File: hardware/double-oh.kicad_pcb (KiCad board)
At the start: 2 copper layers, 81.6 x 14 mm, 42 parts, among them J1 USB_B_Micro, J10 Conn_01x01, J11 Conn_01x01, J2 Conn_01x01, J3 Conn_01x01, J4 Conn_01x01, J5 Conn_01x01, J6 Conn_01x01, J7 Conn_01x01, J8 Conn_01x01, J9 Conn_01x01, Q1 Q_PMOS_GSD, Q2 Q_DUAL_NPN_NPN_E1B1C2E2B2C1, U1 AP2127N-3.3, U2 MCP4017-xxxx, U3 MCP73831-2-OT, U4 LMV321, U5 ESP8285, U6 CP2105, Y1 26MHz

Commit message: Update i2c net names
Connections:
- net digipot_sclk renamed i2c_sda
- net digipot_u~d renamed i2c_scl

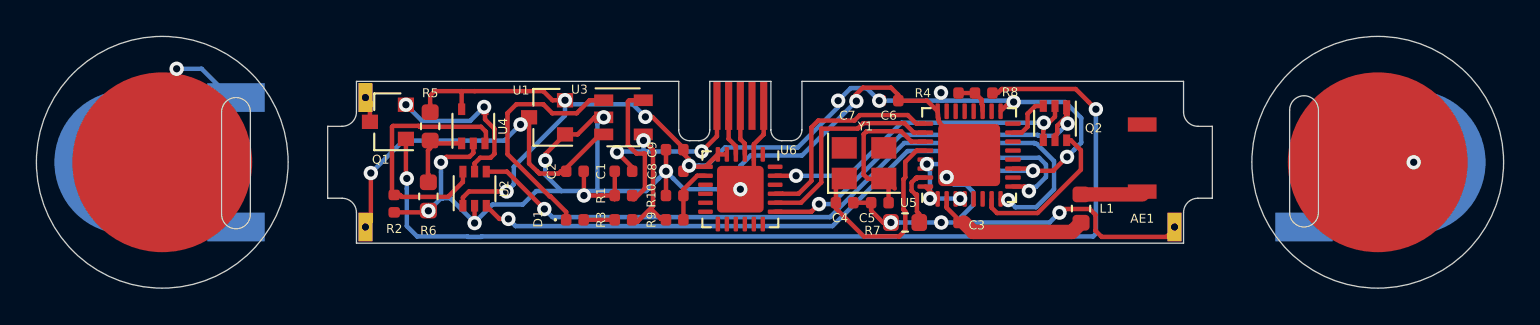
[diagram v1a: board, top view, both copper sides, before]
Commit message: Added a factory-reset pad to hardware
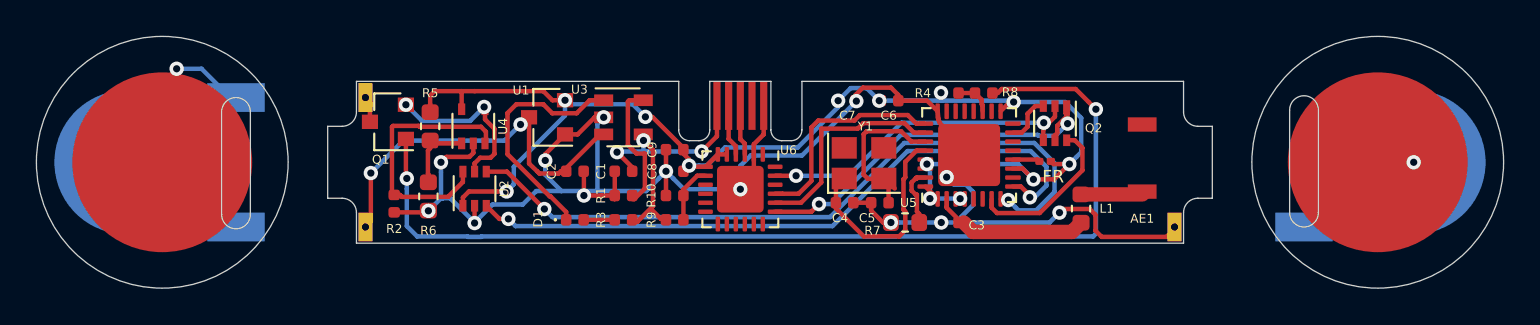
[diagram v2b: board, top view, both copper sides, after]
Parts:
- added FR: 1GΩ, Resistor_SMD:R_0201_0603Metric, F.Cu at (138.3, 104.5)
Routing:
- net 3.3V: track 74.4 -> 76.4 mm
- net Net-(R11-Pad1): track 0.00 -> 1.51 mm
- net i2c_scl: track 36.7 -> 37.3 mm

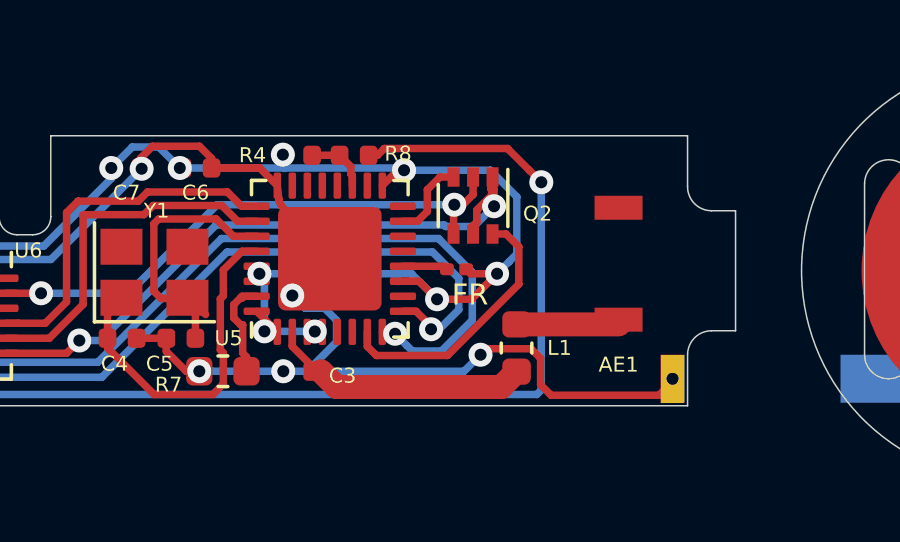
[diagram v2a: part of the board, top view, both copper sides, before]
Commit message: Updated factory reset hardware to work with factory reset firmware
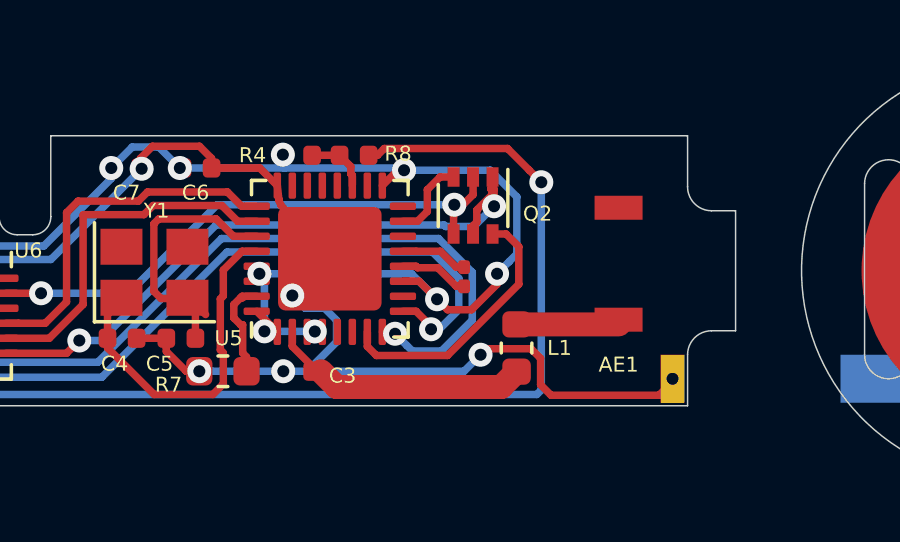
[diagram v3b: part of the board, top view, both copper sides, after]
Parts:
- moved R11 0.35 mm to (138.6, 104.7), turned to 90 degrees
- renumbered FR to R11
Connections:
- R11 pad 2: 3.3V -> Net-(R11-Pad2)
- U5 pad 13: Net-(U5-Pad13) -> Net-(R11-Pad2)
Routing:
- net Net-(R11-Pad2): track 0.00 -> 2.26 mm
- net Net-(R11-Pad1): track 1.51 -> 2.32 mm
- net 3.3V: track 76.4 -> 75.8 mm

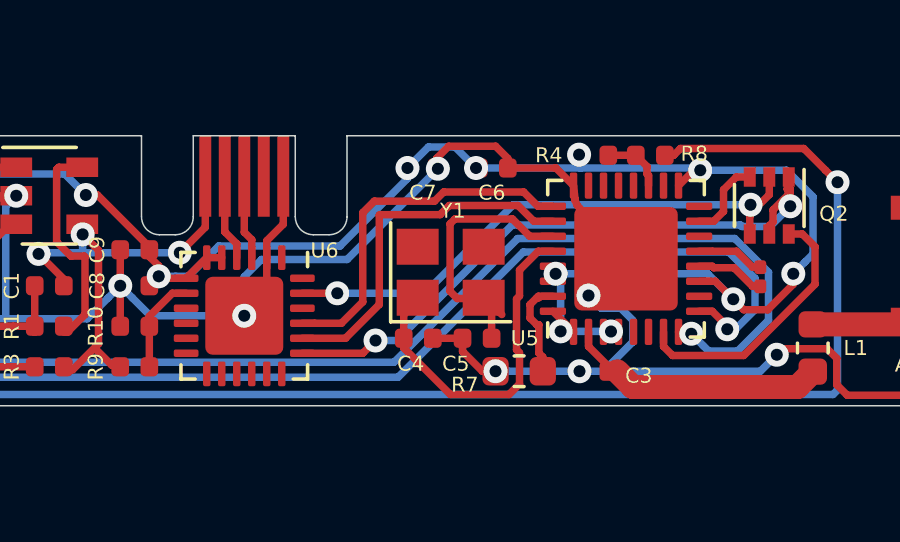
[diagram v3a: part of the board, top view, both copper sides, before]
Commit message: Fixed crystal layout and routing
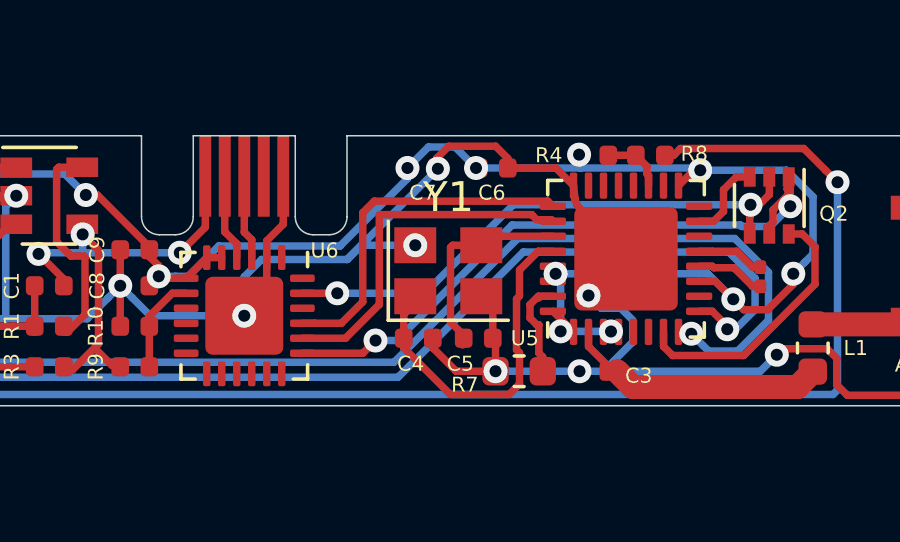
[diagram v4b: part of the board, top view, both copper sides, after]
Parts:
- Y1: value 26MHz -> Crystal_GND24; footprint Crystal:Crystal_SMD_TXC_7M-4Pin_3.2x2.5mm -> Crystal:Crystal_SMD_3225-4Pin_3.2x2.5mm
- moved Y1 0.09 mm to (128.2, 104.5)
- turned C5 to 0 degrees
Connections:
- Y1 pad 2: Net-(C5-Pad1) -> 0V
- Y1 pad 3: (no net) -> Net-(C5-Pad1)
- Y1 pad 4: (no net) -> 0V
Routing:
- net 0V: track 95.7 -> 100.6 mm, vias 13 -> 14
- net Net-(C5-Pad1): track 9.49 -> 7.00 mm

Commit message: Update main board gerbers
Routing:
- net to_top_cap: track 2.02 -> 1.45 mm
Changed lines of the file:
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@@
     (thickness 0.6)
     (drawings 58)
-    (tracks 506)
+    (tracks 505)
     (zones 0)
     (modules 43)
@@
   (segment (start 116.362659 103.687339) (end 115.96266 103.28734) (width 0.25) (layer F.Cu) (net 2))
   (segment (start 115.335 105) (end 115.335 104.780819) (width 0.25) (layer F.Cu) (net 2))
+  (segment (start 128.625 106.75) (end 128.625 106.975) (width 0.25) (layer F.Cu) (net 3))
+  (segment (start 128.3 103.65) (end 129.25 103.65) (width 0.25) (layer F.Cu) (net 3))
+  (segment (start 128.224999 103.725001) (end 128.3 103.65) (width 0.25) (layer F.Cu) (net 3))
+  (segment (start 128.224999 106.210001) (end 128.224999 103.725001) (width 0.25) (layer F.Cu) (net 3))
+  (segment (start 128.665 106.650002) (end 128.224999 106.210001) (width 0.25) (layer F.Cu) (net 3))
+  (segment (start 128.665 106.75) (end 128.665 106.650002) (width 0.25) (layer F.Cu) (net 3))
+  (segment (start 129.55 103.35) (end 129.25 103.65) (width 0.25) (layer F.Cu) (net 3))
+  (segment (start 131.6375 103.35) (end 129.55 103.35) (width 0.25) (layer F.Cu) (net 3))
   (segment (start 114.365 107.7) (end 112.635 107.7) (width 0.25) (layer F.Cu) (net 4))
   (segment (start 112.97 101.05) (end 113.75 101.05) (width 0.25) (layer F.Cu) (net 5))
@@
   (segment (start 111.37 105) (end 111.665 105) (width 0.25) (layer F.Cu) (net 7))
   (via (at 132.525 107.85) (size 0.8) (drill 0.4) (layers F.Cu B.Cu) (net 8))
-  (via (at 106.57 107.88) (size 0.8) (drill 0.4) (layers F.Cu B.Cu) (net 8))
   (via (at 104.7 104.5) (size 0.8) (drill 0.4) (layers F.Cu B.Cu) (net 8))
   (via (at 110.5 104.4) (size 0.8) (drill 0.4) (layers F.Cu B.Cu) (net 8))
@@
   (segment (start 140.781484 107.09999) (end 141.10001 107.418516) (width 0.25) (layer F.Cu) (net 8))
   (segment (start 106.5 103.6) (end 106.5 103.98359) (width 0.25) (layer F.Cu) (net 8))
-  (segment (start 106.57 107.85) (end 106.57 107.88) (width 0.25) (layer B.Cu) (net 8))
   (segment (start 110 106.1) (end 109.25 106.85) (width 0.25) (layer B.Cu) (net 8))
   (segment (start 138.55 107.85) (end 139.1 107.3) (width 0.25) (layer B.Cu) (net 8))
@@
   (segment (start 110.5 104.4) (end 110.5 104.05) (width 0.25) (layer F.Cu) (net 8))
   (segment (start 106.5 103.98359) (end 106.28359 104.2) (width 0.25) (layer F.Cu) (net 8))
-  (segment (start 106.57 107.88) (end 106.57 106.92) (width 0.25) (layer F.Cu) (net 8))
   (segment (start 104.8 106.5) (end 104.7 106.4) (width 0.25) (layer B.Cu) (net 8))
   (segment (start 110.5 104.4) (end 110.5 105.2) (width 0.25) (layer B.Cu) (net 8))
@@
   (segment (start 117.215972 104.025972) (end 117.215 104.025) (width 0.25) (layer F.Cu) (net 8))
   (segment (start 124.777644 104.12501) (end 121.92499 104.12501) (width 0.25) (layer B.Cu) (net 8))
-  (segment (start 128.625 106.75) (end 128.625 106.975) (width 0.25) (layer F.Cu) (net 3))
-  (segment (start 128.3 103.65) (end 129.25 103.65) (width 0.25) (layer F.Cu) (net 3))
-  (segment (start 128.224999 103.725001) (end 128.3 103.65) (width 0.25) (layer F.Cu) (net 3))
-  (segment (start 128.224999 106.210001) (end 128.224999 103.725001) (width 0.25) (layer F.Cu) (net 3))
-  (segment (start 128.665 106.650002) (end 128.224999 106.210001) (width 0.25) (layer F.Cu) (net 3))
-  (segment (start 128.665 106.75) (end 128.665 106.650002) (width 0.25) (layer F.Cu) (net 3))
-  (segment (start 129.55 103.35) (end 129.25 103.65) (width 0.25) (layer F.Cu) (net 3))
-  (segment (start 131.6375 103.35) (end 129.55 103.35) (width 0.25) (layer F.Cu) (net 3))
   (segment (start 134.299001 106.874001) (end 134.300001 106.873001) (width 0.25) (layer B.Cu) (net 8))
   (segment (start 122.1 105.25) (end 121.35 106) (width 0.25) (layer F.Cu) (net 8))
@@
   (segment (start 125.252654 103.65) (end 127.05 103.65) (width 0.25) (layer B.Cu) (net 8))
   (segment (start 124.777644 104.12501) (end 125.252654 103.65) (width 0.25) (layer B.Cu) (net 8))
+  (segment (start 106.57 107.85) (end 106.57 107.88) (width 0.25) (layer B.Cu) (net 8))
+  (via (at 106.57 107.88) (size 0.8) (drill 0.4) (layers F.Cu B.Cu) (net 8))
+  (segment (start 106.57 107.88) (end 106.57 106.92) (width 0.25) (layer F.Cu) (net 8))
   (segment (start 128.22 108.625) (end 130.175 108.625) (width 0.25) (layer F.Cu) (net 9))
   (segment (start 130.42498 107.13639) (end 130.52499 107.2364) (width 0.25) (layer F.Cu) (net 9))
@@
   (via (at 102.8 105.4) (size 0.8) (drill 0.4) (layers F.Cu B.Cu) (net 14))
   (via (at 141.125 101.55) (size 0.8) (drill 0.4) (layers F.Cu B.Cu) (net 14))
-  (segment (start 103.375 108.625) (end 102.8 108.05) (width 0.25) (layer B.Cu) (net 14))
-  (segment (start 140.975 108.625) (end 106.968004 108.625) (width 0.25) (layer B.Cu) (net 14))
-  (segment (start 141.125 108.475) (end 140.975 108.625) (width 0.25) (layer B.Cu) (net 14))
-  (segment (start 106.943014 108.64999) (end 106.196986 108.64999) (width 0.25) (layer B.Cu) (net 14))
-  (segment (start 106.196986 108.64999) (end 106.171996 108.625) (width 0.25) (layer B.Cu) (net 14))
-  (segment (start 102.8 108.05) (end 102.8 105.965685) (width 0.25) (layer B.Cu) (net 14))
-  (segment (start 102.8 105.965685) (end 102.8 105.4) (width 0.25) (layer B.Cu) (net 14))
-  (segment (start 141.125 101.55) (end 141.125 108.475) (width 0.25) (layer B.Cu) (net 14))
-  (segment (start 106.171996 108.625) (end 103.375 108.625) (width 0.25) (layer B.Cu) (net 14))
   (segment (start 135.37 100.65) (end 135.665 100.65) (width 0.25) (layer F.Cu) (net 14))
   (segment (start 139.999999 100.424999) (end 140.725001 101.150001) (width 0.25) (layer F.Cu) (net 14))
   (segment (start 135.665 100.65) (end 135.890001 100.424999) (width 0.25) (layer F.Cu) (net 14))
   (segment (start 102.75 103.2) (end 102.75 105.35) (width 0.25) (layer F.Cu) (net 14))
-  (segment (start 106.968004 108.625) (end 106.943014 108.64999) (width 0.25) (layer B.Cu) (net 14))
   (segment (start 140.725001 101.150001) (end 141.125 101.55) (width 0.25) (layer F.Cu) (net 14))
   (segment (start 135.890001 100.424999) (end 139.999999 100.424999) (width 0.25) (layer F.Cu) (net 14))
   (segment (start 102.75 105.35) (end 102.8 105.4) (width 0.25) (layer F.Cu) (net 14))
+  (segment (start 106.943014 108.64999) (end 106.196986 108.64999) (width 0.25) (layer B.Cu) (net 14))
+  (segment (start 106.968004 108.625) (end 106.943014 108.64999) (width 0.25) (layer B.Cu) (net 14))
+  (segment (start 141.125 101.55) (end 141.125 108.475) (width 0.25) (layer B.Cu) (net 14))
+  (segment (start 106.196986 108.64999) (end 106.171996 108.625) (width 0.25) (layer B.Cu) (net 14))
+  (segment (start 140.975 108.625) (end 106.968004 108.625) (width 0.25) (layer B.Cu) (net 14))
+  (segment (start 102.8 105.965685) (end 102.8 105.4) (width 0.25) (layer B.Cu) (net 14))
+  (segment (start 141.125 108.475) (end 140.975 108.625) (width 0.25) (layer B.Cu) (net 14))
+  (segment (start 106.171996 108.625) (end 103.375 108.625) (width 0.25) (layer B.Cu) (net 14))
+  (segment (start 103.375 108.625) (end 102.8 108.05) (width 0.25) (layer B.Cu) (net 14))
+  (segment (start 102.8 108.05) (end 102.8 105.965685) (width 0.25) (layer B.Cu) (net 14))
   (via (at 107.1 101.425) (size 0.8) (drill 0.4) (layers F.Cu B.Cu) (net 15))
   (segment (start 107.15 102.11359) (end 107.675001 102.638591) (width 0.25) (layer F.Cu) (net 15))
@@
   (segment (start 158.8 104.5) (end 154.800001 108.499999) (width 0.25) (layer B.Cu) (net 53))
   (segment (start 153.099999 108.499999) (end 153.014102 108.414101) (width 0.25) (layer B.Cu) (net 53))
-  (segment (start 100.9 101.3) (end 100.5 100.9) (width 0.25) (layer F.Cu) (net 54))
   (segment (start 100.75 101.15) (end 100.5 100.9) (width 0.25) (layer F.Cu) (net 54))
   (segment (start 100.75 102.25) (end 100.75 101.15) (width 0.25) (layer F.Cu) (net 54))

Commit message: Update crystal caps
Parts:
- C4, C5: value 5.6pF -> 10pF
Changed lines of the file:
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@@
       (effects (font (size 0.5 0.5) (thickness 0.1)))
     )
-    (fp_text value 5.6pF (at 0 1.17) (layer F.Fab)
+    (fp_text value 10pF (at 0 1.17) (layer F.Fab)
       (effects (font (size 1 1) (thickness 0.15)))
     )
@@
       (effects (font (size 0.5 0.5) (thickness 0.1)))
     )
-    (fp_text value 5.6pF (at 0 1.17) (layer F.Fab)
+    (fp_text value 10pF (at 0 1.17) (layer F.Fab)
       (effects (font (size 1 1) (thickness 0.15)))
     )

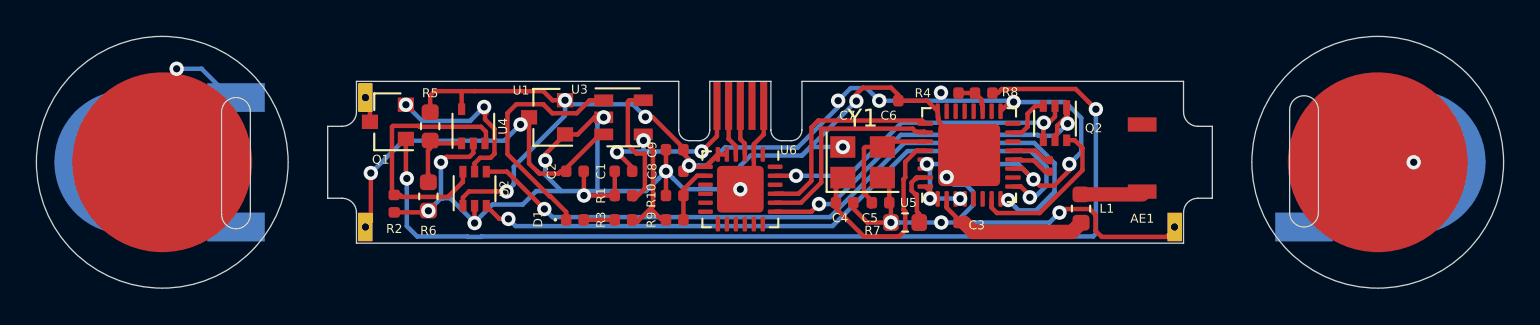
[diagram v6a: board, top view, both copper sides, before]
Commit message: Increased text size for legibility
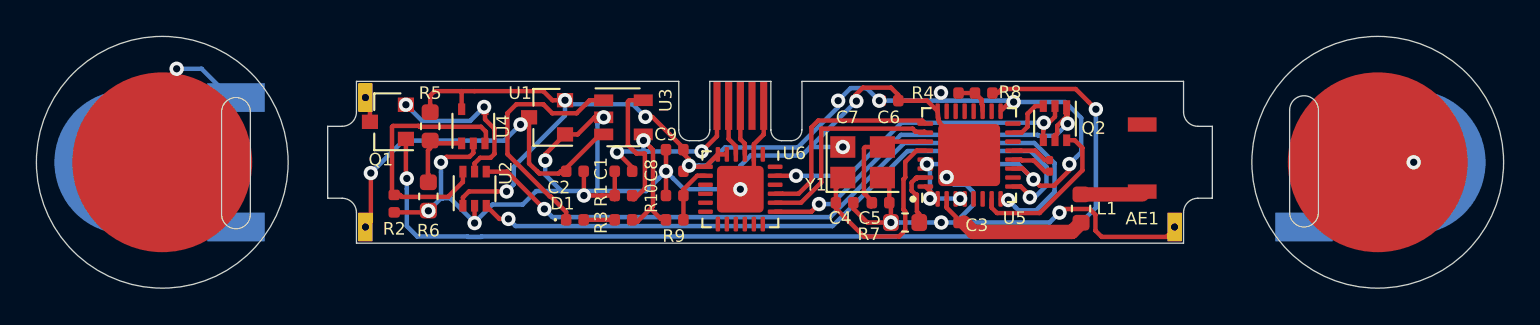
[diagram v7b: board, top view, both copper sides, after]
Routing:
- net Net-(Q1-Pad1): track 56.8 -> 55.9 mm

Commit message: Working on a version that, y'know, would actually work
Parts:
- removed the R2 at (102.1, 106.8)
- removed the R5 at (104.1, 102.5)
- removed the R6 at (104.0, 106.4)
- removed the U3 at (114.8, 102.0)
- removed the U4 at (106.5, 102.5)
- added ?: Conn_01x01, powerplay:cap_board_solder_mount, B.Cu at (152.7, 100.9)
- added ?: Conn_01x01, powerplay:main_board_solder_mount, F.Cu at (145.5, 100.9)
- added C10: 10μF, Capacitor_SMD:C_0402_1005Metric, F.Cu at (108.7, 104.0)
- added C11: 4.7μF, Capacitor_SMD:C_0402_1005Metric, F.Cu at (106.7, 107.8)
- added C12: 4.7μF, Capacitor_SMD:C_0402_1005Metric, F.Cu at (105.8, 102.4)
- added C13: 10μF, Capacitor_SMD:C_0402_1005Metric, F.Cu at (104.1, 106.0)
- added L2: 2.2 μH, Inductor_SMD:L_0402_1005Metric, F.Cu at (108.7, 106.1)
- added L3: 2.2 μH, Inductor_SMD:L_0402_1005Metric, F.Cu at (104.1, 104.0)
- added R10: 67 kΩ, Resistor_SMD:R_0402_1005Metric, F.Cu at (107.0, 100.7)
- added R11: 100 kΩ, Resistor_SMD:R_0402_1005Metric, F.Cu at (103.0, 106.0)
- added R9: 300 kΩ, Resistor_SMD:R_0402_1005Metric, F.Cu at (108.8, 101.8)
- added U5: MP2109, Package_DFN_QFN:DFN-10-1EP_3x3mm_P0.5mm_EP1.7x2.5mm, F.Cu at (106.3, 105.0)
- U1: value AP2127N-3.3 -> MCP73831-2-OT; footprint Package_TO_SOT_SMD:SOT-23 -> Package_TO_SOT_SMD:SOT-23-5
- moved U3 4.73 mm to (111.3, 105.8), turned to 0 degrees
- moved U1 4.25 mm to (114.8, 102.0), turned to 0 degrees
- moved C2 2.57 mm to (112.5, 102.5), turned to 270 degrees
- moved D1 1.27 mm to (113.4, 107.7)
- moved R4 0.67 mm to (115.5, 107.7)
- renumbered C8 to C3, C9 to C4, C6 to C5, C7 to C6, C3 to C7, C4 to C8, C5 to C9, Q2 to Q1, Q1 to Q2, R9 to R1, R1 to R2, R10 to R3, R3 to R4, R7 to R5, R11 to R6, R4 to R7, U6 to U2, U2 to U3, U5 to U4
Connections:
- R2 pad 2: Net-(R1-Pad2) (its old number) -> Net-(R2-Pad2)
- U1 pad 1: 0V -> Net-(D1-Pad1)
- U1 pad 2: 3.3V -> 0V
- U2 pad 5: Net-(U6-Pad5) -> 3.3V
- U3 pad 5: batt_out -> digipot2
- U3 pad 6: digipot1 -> 0V
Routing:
- net digipot1: track 14.8 -> 0.00 mm
- net digipot2: track 0.00 -> 14.7 mm, vias 0 -> 3
- net 3.3V: track 75.8 -> 65.5 mm, vias 13 -> 12
- net LIPO_V: track 21.2 -> 30.4 mm, vias 2 -> 3
- net Net-(R1-Pad2) (its old number): track 7.32 -> 0.00 mm
- net Net-(R2-Pad2): track 0.00 -> 7.01 mm
- net 0V: track 100.6 -> 94.6 mm, vias 14 -> 12
- net i2c_sda: track 40.1 -> 34.9 mm
- net Net-(D1-Pad1): track 13.4 -> 8.19 mm
- net Net-(R10-Pad1): track 0.00 -> 4.80 mm, vias 0 -> 2
- net Net-(R5-Pad2) (its old number): track 4.65 -> 0.00 mm
- net USB_VIN: track 16.6 -> 14.6 mm
- net i2c_scl: track 37.3 -> 35.8 mm
- net Net-(L2-Pad2): track 0.00 -> 1.34 mm
- net Net-(L3-Pad1): track 0.00 -> 1.28 mm
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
